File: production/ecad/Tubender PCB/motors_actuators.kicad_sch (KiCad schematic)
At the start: 0 parts

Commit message: MCU Rev1 Complete
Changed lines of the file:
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@@
+		)
+	)
+	(global_label "BENDING_ENA"
+		(shape input)
+		(at 44.45 86.36 180)
+		(fields_autoplaced yes)
+		(effects
+			(font
+				(size 1.27 1.27)
+			)
+			(justify right)
+		)
+		(property "Intersheetrefs" "${INTERSHEET_REFS}"
+			(at 28.7043 86.36 0)
+			(effects
+				(font
+					(size 1.27 1.27)
+				)
+				(justify right)
+				(hide yes)
+			)
 		)
 	)

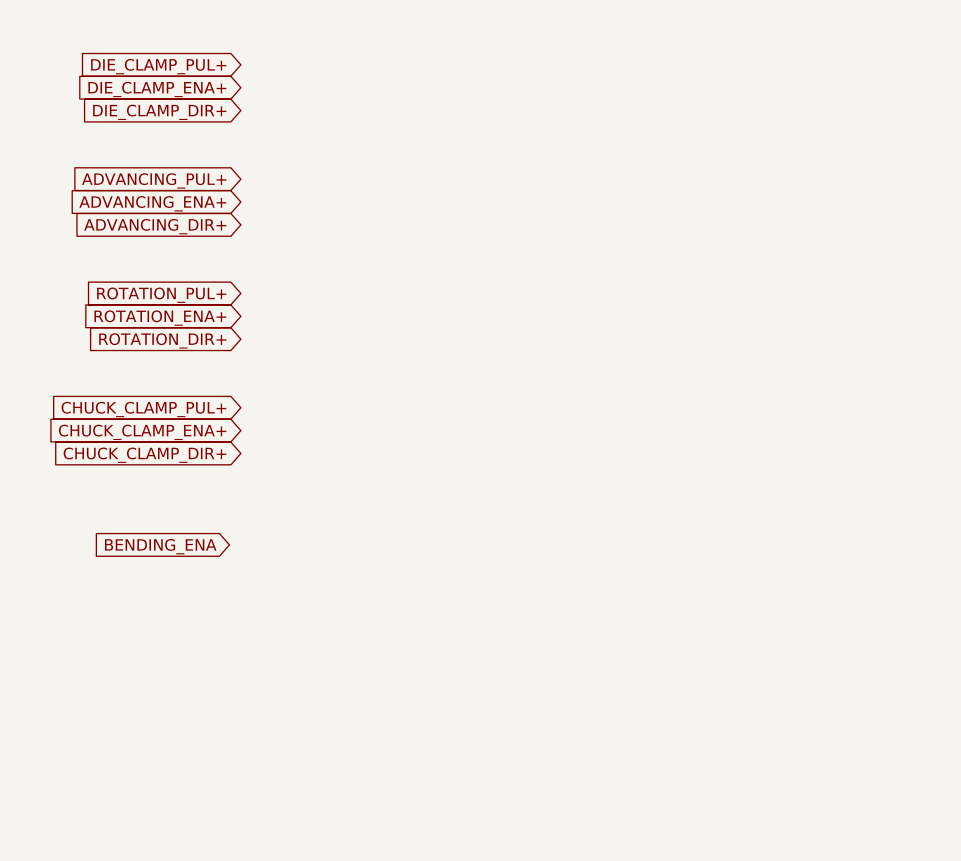
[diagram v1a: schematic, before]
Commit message: Added Motor Connectors
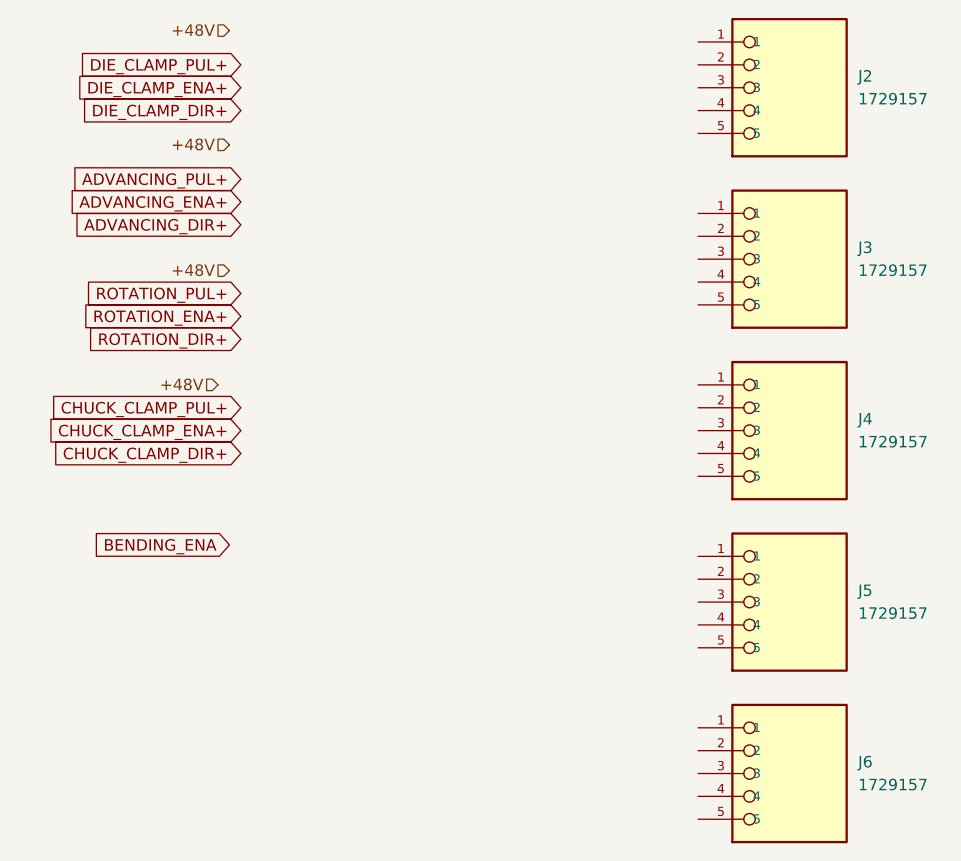
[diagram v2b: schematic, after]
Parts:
- added J2, J3, J4, J5, J6: 1729157, 1729157:PHOENIX_1729157, symbol 1729157:1729157

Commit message: Motor Page
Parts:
- removed J6: 1729157, 1729157:PHOENIX_1729157, symbol 1729157:1729157
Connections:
- net +48V: now also J2.1, J3.1, J4.1, J5.1
- net ADVANCING_DIR+: now also J3.4
- net ADVANCING_ENA+: now also J3.3
- net ADVANCING_PUL+: now also J3.2
- net CHUCK_CLAMP_DIR+: now also J5.4
- net CHUCK_CLAMP_ENA+: now also J5.3
- net CHUCK_CLAMP_PUL+: now also J5.2
- net DIE_CLAMP_DIR+: now also J2.4
- net DIE_CLAMP_ENA+: now also J2.3
- net DIE_CLAMP_PUL+: now also J2.2
- net ROTATION_DIR+: now also J4.4
- net ROTATION_ENA+: now also J4.3
- net ROTATION_PUL+: now also J4.2
- net GND: now reaches J4.5
- net GND: now also J2.5, J3.5, J5.5
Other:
- note added: "Advancing Motor Connector"
- note added: "Bending Actuator Connector"
- note added: "Chuck Clamp Motor Connector"
- note added: "Die Clamp Motor Connector"
- note added: "Rotation Motor Connector"
- moved on the sheet: J2, J3, J4, J5

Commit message: 8 connector
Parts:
- added J6: 1729186, 1729186:PHOENIX_1729186, symbol 1729186:1729186
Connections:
- net GND: now also J6.2, J6.8
- new net 12V: J6.1
- new net 5V: J6.7
- new net BENDING_LPWM: J6.5
- new net BENDING_L_ENA: J6.3
- new net BENDING_RPWM: J6.6
- new net BENDING_R_ENA: J6.4

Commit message: Formatting
Boom
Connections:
- net 5V is gone; now on net GND: J6.7
- net BENDING_LPWM is gone; now on net GND: J6.5
- net BENDING_L_ENA is gone; now on net GND: J6.3
- net BENDING_RPWM is gone; now on net GND: J6.6
- net BENDING_R_ENA is gone; now on net GND: J6.4
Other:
- moved on the sheet: J2, J3, J4, J5, J6

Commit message: final for rev 1
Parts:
- removed J2, J3, J4, J5: 1729157, 1729157:PHOENIX_1729157, symbol 1729157:1729157
- removed J6: 1729186, 1729186:PHOENIX_1729186, symbol 1729186:1729186
- added J14, J2, J3, J4: 640445-5, 640445-5:TE_640445-5, symbol 640445-5:640445-5
- added J6: 640445-6, 640445-6:TE_640445-6, symbol 640445-6:640445-6
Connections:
- net +48V: now also J14.1, J2.1, J3.1, J4.1
- net ADVANCING_DIR+: now also J2.4
- net ADVANCING_ENA+: now also J2.3
- net ADVANCING_PUL+: now also J2.2
- net CHUCK_CLAMP_DIR+: now also J4.4
- net CHUCK_CLAMP_ENA+: now also J4.3
- net CHUCK_CLAMP_PUL+: now also J4.2
- net DIE_CLAMP_DIR+: now also J14.4
- net DIE_CLAMP_ENA+: now also J14.3
- net DIE_CLAMP_PUL+: now also J14.2
- net GND: now also J14.5, J2.5, J3.5, J4.5, J6.6
- net ROTATION_DIR+: now also J3.4
- net ROTATION_ENA+: now also J3.3
- net ROTATION_PUL+: now also J3.2
- new net 24V: J6.1
- new net BENDING_LPWM: J6.4
- new net BENDING_L_ENA: J6.2
- new net BENDING_RPWM: J6.5
- new net BENDING_R_ENA: J6.3

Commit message: Fixed Button Connectors
All done! Enjoy :)
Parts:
- removed J14, J2, J3, J4: 640445-5, 640445-5:TE_640445-5, symbol 640445-5:640445-5
- removed J6: 640445-6, 640445-6:TE_640445-6, symbol 640445-6:640445-6
- added J11: 640387-8, 640387-8:TE_640387-8, symbol 640387-8:640387-8
- added J13, J2, J3, J4: 640387-5, 640387-5:TE_640387-5, symbol 640387-5:640387-5
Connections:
- net +48V: now also J13.1, J2.1, J3.1, J4.1
- net ADVANCING_DIR+: now also J3.4
- net ADVANCING_ENA+: now also J3.3
- net ADVANCING_PUL+: now also J3.2
- net BENDING_LPWM: now also J11.5
- net BENDING_L_ENA: now also J11.3
- net BENDING_RPWM: now also J11.6
- net BENDING_R_ENA: now also J11.4
- net CHUCK_CLAMP_DIR+: now also J13.4
- net CHUCK_CLAMP_ENA+: now also J13.3
- net CHUCK_CLAMP_PUL+: now also J13.2
- net DIE_CLAMP_DIR+: now also J2.4
- net DIE_CLAMP_ENA+: now also J2.3
- net DIE_CLAMP_PUL+: now also J2.2
- net GND: now also J11.2, J11.8, J13.5, J2.5, J3.5, J4.5
- net ROTATION_DIR+: now also J4.4
- net ROTATION_ENA+: now also J4.3
- net ROTATION_PUL+: now also J4.2
- new net 12V: J11.1
- new net 5V: J11.7
